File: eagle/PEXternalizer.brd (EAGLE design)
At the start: 50 x 50 mm, 11 parts, among them X1 22-23-2031, X2 22-23-2041

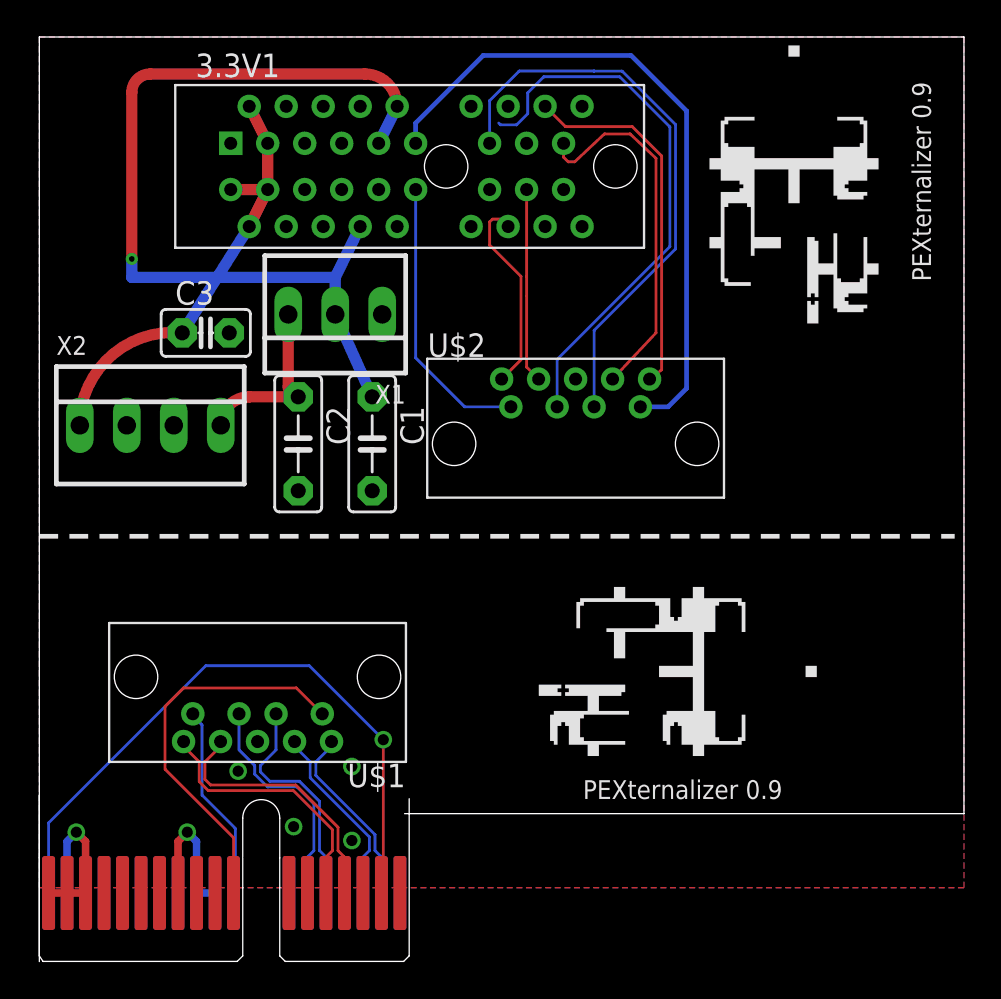
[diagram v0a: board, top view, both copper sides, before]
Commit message: Fixed stupid board error.
overlapping power plane traces fixed!
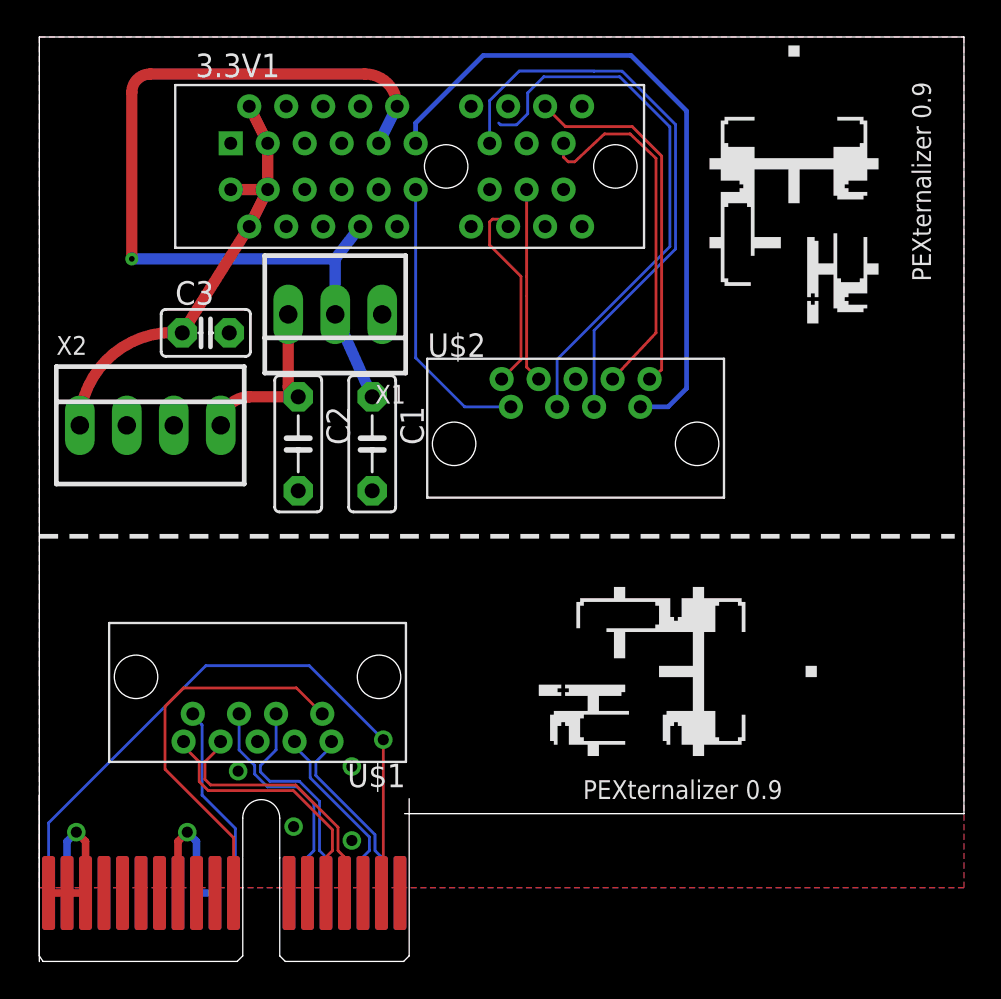
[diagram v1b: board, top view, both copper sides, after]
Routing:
- net 3.3V1: track 48.7 -> 47.8 mm
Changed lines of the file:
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@@
 </class>
 </classes>
-<designrules name="LaenPCBOrder">
-<description language="de">&lt;b&gt;EAGLE Design Rules&lt;/b&gt;
+<designrules name="DFRobot_Eagle_Rule_v0.4">
+<description language="en">
+&lt;b&gt;EAGLE Design Rules&lt;/b&gt;
 &lt;p&gt;
-Die Standard-Design-Rules sind so gewählt, dass sie für
-die meisten Anwendungen passen. Sollte ihre Platine
-besondere Anforderungen haben, treffen Sie die erforderlichen
-Einstellungen hier und speichern die Design Rules unter
-einem neuen Namen ab.</description>
-<description language="en">&lt;b&gt;Laen's PCB Order Design Rules&lt;/b&gt;
+The default Design Rules have been set to cover
+a wide range of applications. Your particular design
+may have different requirements, so please make the
+necessary adjustments and save your customized
+design rules under a new name.
+</description>
+<description language="it">
+&lt;b&gt;EAGLE Design Rules&lt;/b&gt;
 &lt;p&gt;
-Please make sure your boards conform to these design rules.</description>
+The default Design Rules have been set to cover
+a wide range of applications. Your particular design
+may have different requirements, so please make the
+necessary adjustments and save your customized
+design rules under a new name.</description>
 <param name="layerSetup" value="(1*16)"/>
-<param name="mtCopper" value="0.0356mm 0.0356mm 0.0356mm 0.0356mm 0.0356mm 0.0356mm 0.0356mm 0.0356mm 0.0356mm 0.0356mm 0.0356mm 0.0356mm 0.0356mm 0.0356mm 0.0356mm 0.0356mm"/>
-<param name="mtIsolate" value="1.5011mm 0.1499mm 0.2007mm 0.1499mm 0.2007mm 0.1499mm 0.2007mm 0.1499mm 0.2007mm 0.1499mm 0.2007mm 0.1499mm 0.2007mm 0.1499mm 0.2007mm"/>
+<param name="mtCopper" value="0.035mm 0.035mm 0.035mm 0.035mm 0.035mm 0.035mm 0.035mm 0.035mm 0.035mm 0.035mm 0.035mm 0.035mm 0.035mm 0.035mm 0.035mm 0.035mm"/>
+<param name="mtIsolate" value="1.5mm 0.15mm 0.2mm 0.15mm 0.2mm 0.15mm 0.2mm 0.15mm 0.2mm 0.15mm 0.2mm 0.15mm 0.2mm 0.15mm 0.2mm"/>
 <param name="mdWireWire" value="6mil"/>
 <param name="mdWirePad" value="6mil"/>
@@
 <param name="mdPadVia" value="6mil"/>
 <param name="mdViaVia" value="6mil"/>
-<param name="mdSmdPad" value="6mil"/>
-<param name="mdSmdVia" value="6mil"/>
-<param name="mdSmdSmd" value="6mil"/>
+<param name="mdSmdPad" value="0mil"/>
+<param name="mdSmdVia" value="0mil"/>
+<param name="mdSmdSmd" value="0mil"/>
 <param name="mdViaViaSameLayer" value="8mil"/>
 <param name="mnLayersViaInSmd" value="2"/>
-<param name="mdCopperDimension" value="15mil"/>
-<param name="mdDrill" value="6mil"/>
+<param name="mdCopperDimension" value="10mil"/>
+<param name="mdDrill" value="10mil"/>
 <param name="mdSmdStop" value="0mil"/>
 <param name="msWidth" value="6mil"/>
-<param name="msDrill" value="13mil"/>
-<param name="msMicroVia" value="13mil"/>
+<param name="msDrill" value="12mil"/>
+<param name="msMicroVia" value="12mil"/>
 <param name="msBlindViaRatio" value="0.5"/>
 <param name="rvPadTop" value="0.25"/>
@@
 <param name="rvMicroViaOuter" value="0.25"/>
 <param name="rvMicroViaInner" value="0.25"/>
-<param name="rlMinPadTop" value="7mil"/>
+<param name="rlMinPadTop" value="12mil"/>
 <param name="rlMaxPadTop" value="20mil"/>
-<param name="rlMinPadInner" value="7mil"/>
+<param name="rlMinPadInner" value="10mil"/>
 <param name="rlMaxPadInner" value="20mil"/>
-<param name="rlMinPadBottom" value="7mil"/>
+<param name="rlMinPadBottom" value="12mil"/>
 <param name="rlMaxPadBottom" value="20mil"/>
-<param name="rlMinViaOuter" value="7mil"/>
+<param name="rlMinViaOuter" value="8mil"/>
 <param name="rlMaxViaOuter" value="20mil"/>
-<param name="rlMinViaInner" value="7mil"/>
+<param name="rlMinViaInner" value="8mil"/>
 <param name="rlMaxViaInner" value="20mil"/>
 <param name="rlMinMicroViaOuter" value="4mil"/>
@@
 <param name="mvStopFrame" value="1"/>
 <param name="mvCreamFrame" value="0"/>
-<param name="mlMinStopFrame" value="3mil"/>
-<param name="mlMaxStopFrame" value="3mil"/>
+<param name="mlMinStopFrame" value="2mil"/>
+<param name="mlMaxStopFrame" value="2mil"/>
 <param name="mlMinCreamFrame" value="0mil"/>
 <param name="mlMaxCreamFrame" value="0mil"/>
-<param name="mlViaStopLimit" value="0mil"/>
+<param name="mlViaStopLimit" value="25mil"/>
 <param name="srRoundness" value="0"/>
 <param name="srMinRoundness" value="0mil"/>
@@
 <via x="5" y="38" extent="1-16" drill="0.3048"/>
 <wire x1="19.35" y1="46.25" x2="18.35" y2="44.25" width="0.6096" layer="16"/>
-<wire x1="16" y1="35" x2="16" y2="37" width="0.6096" layer="16"/>
-<wire x1="16" y1="37" x2="5" y2="37" width="0.6096" layer="16"/>
-<wire x1="5" y1="38" x2="5" y2="37" width="0.6096" layer="16"/>
-<wire x1="17.35" y1="39.75" x2="16" y2="37" width="0.6096" layer="16"/>
+<wire x1="16" y1="35" x2="16" y2="38" width="0.6096" layer="16"/>
+<wire x1="16" y1="38" x2="5" y2="38" width="0.6096" layer="16"/>
+<wire x1="17.35" y1="39.75" x2="16" y2="38" width="0.6096" layer="16"/>
 <wire x1="16" y1="35" x2="18" y2="30.54" width="0.6096" layer="16"/>
 </signal>
@@
 <wire x1="12.35" y1="44.25" x2="11.35" y2="46.25" width="0.6096" layer="1"/>
 <wire x1="12.35" y1="41.75" x2="11.35" y2="39.75" width="0.6096" layer="1"/>
+<wire x1="2.19" y1="29.46" x2="2.19" y2="29" width="0.6096" layer="1"/>
 <wire x1="7.73" y1="34" x2="2.19" y2="29.46" width="0.6096" layer="1" curve="90"/>
-<wire x1="2.19" y1="29.46" x2="2.19" y2="29" width="0.6096" layer="1"/>
-<wire x1="11.35" y1="39.75" x2="7.73" y2="34" width="0.6096" layer="16"/>
+<wire x1="11.35" y1="39.75" x2="7.73" y2="34" width="0.6096" layer="1"/>
 </signal>
 <signal name="N$8">
